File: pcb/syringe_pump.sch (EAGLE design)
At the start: 2 parts, among them U1 R-785.0-0.5

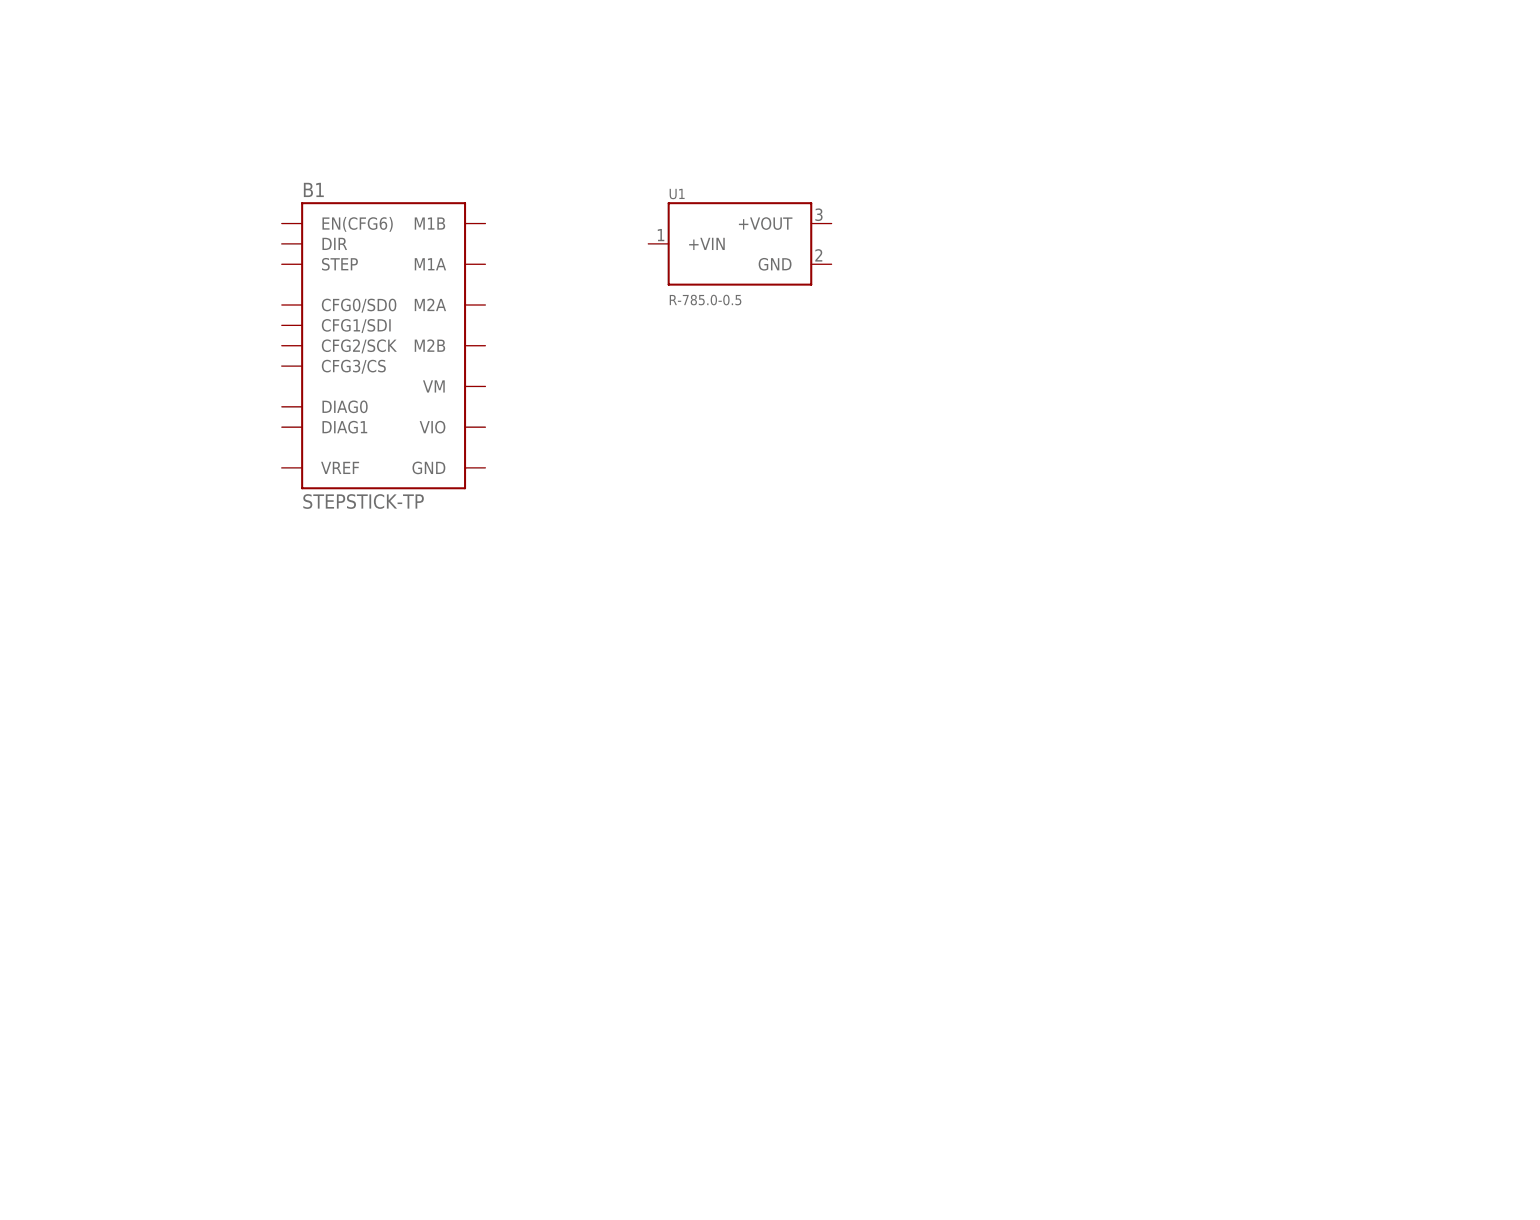
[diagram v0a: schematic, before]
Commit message: Completed syringe pump board and schematic.
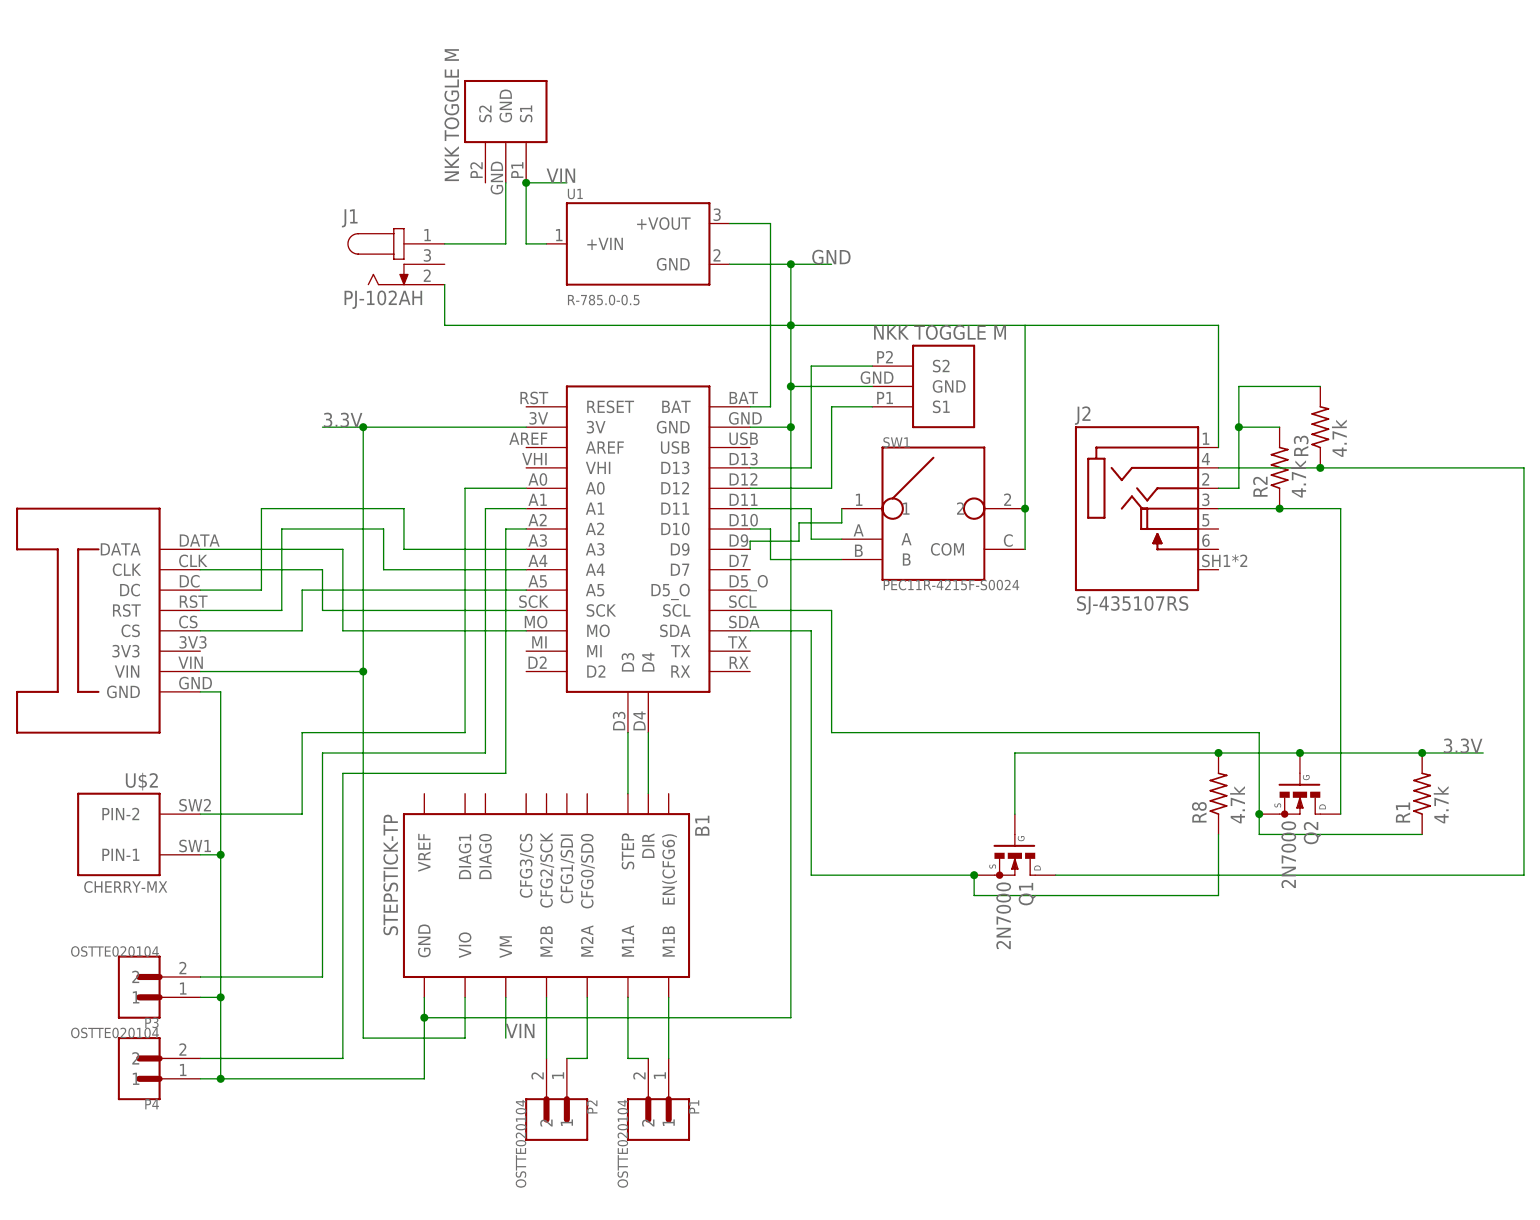
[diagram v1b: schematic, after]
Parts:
- added J1: PJ-102AH, PJ-102AH:PJ-102AH
- added J2: SJ-435107RS, SJ-435107RS:SJ-435107RS
- added P1, P2, P3, P4: OSTTE020104, OSTTE020104:OSTTE020104
- added Q1, Q2: 2N7000, 2N7000:2N7000
- added R1, R2, R3, R8: 4.7k, rcl:R-US_0207/10
- added SW1: PEC11R-4215F-S0024, PEC11R-4215F-S0024:PEC11R-4215F-S0024
- added U$1: ITSYBITSYM4, arthur:ITSYBITSYM4
- added U$2: CHERRY-MX, cherrymx:CHERRY-MX
- added U$3: OLED_128X64, arthur:OLED_128X64
- added U$4: NKK_M2012S2A2A30, arthur:NKK_M2012S2A2A30
- added U$5: NKK_B13AH, arthur:NKK_B13AH
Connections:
- new net 3.3V: B1.VIO, Q1.G, Q2.G, R1.2, R8.2, U$1.3V, U$3.VIN
- new net GND: B1.GND, J1.2, J2.SLEEVE, P3.1, P4.1, SW1.2, SW1.COM, U$1.GND, U$2.PIN-1, U$3.GND, U$5.GND, U1.GND
- new net N$1: Q1.S, R8.1, U$1.SDA
- new net N$10: J2.RING1, Q2.D, R2.1
- new net N$11: J2.RING2, Q1.D, R3.1
- new net N$12: U$1.MO, U$3.DATA
- new net N$13: U$1.A3, U$3.DC
- new net N$14: U$1.A5, U$3.CS
- new net N$15: U$1.A4, U$3.RST
- new net N$16: P4.2, U$1.A2
- new net N$17: U$1.SCK, U$3.CLK
- new net N$18: J1.1, U$4.GND
- new net N$19: P3.2, U$1.A1
- new net N$2: J2.TIP, R2.2, R3.2
- new net N$20: U$1.A0, U$2.PIN-2
- new net N$21: U$1.D12, U$5.S1
- new net N$22: U$1.D13, U$5.S2
- new net N$23: SW1.A, U$1.D11
- new net N$24: SW1.B, U$1.D10
- new net N$25: SW1.1, U$1.D9
- new net N$26: U$1.BAT, U1.+VOUT
- new net N$3: B1.STEP, U$1.D3
- new net N$4: B1.DIR, U$1.D4
- new net N$5: Q2.S, R1.1, U$1.SCL
- new net N$6: B1.M2B, P2.2
- new net N$7: B1.M2A, P2.1
- new net N$8: B1.M1B, P1.1
- new net N$9: B1.M1A, P1.2
- new net VIN: B1.VM, U$4.S1, U1.+VIN
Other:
- moved on the sheet: B1, U1

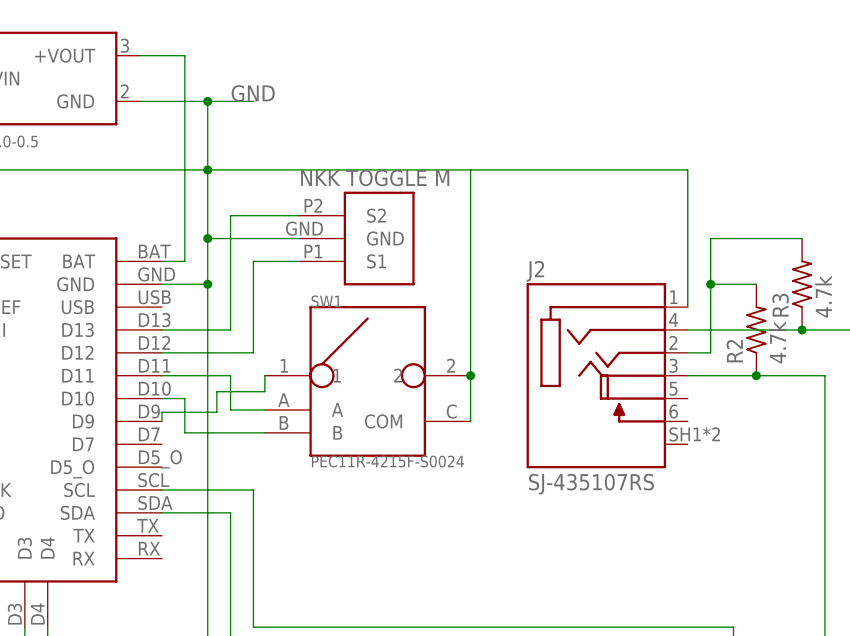
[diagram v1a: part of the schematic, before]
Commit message: Updated spacing of syringe pump and added copy of encoder library due to version issues.
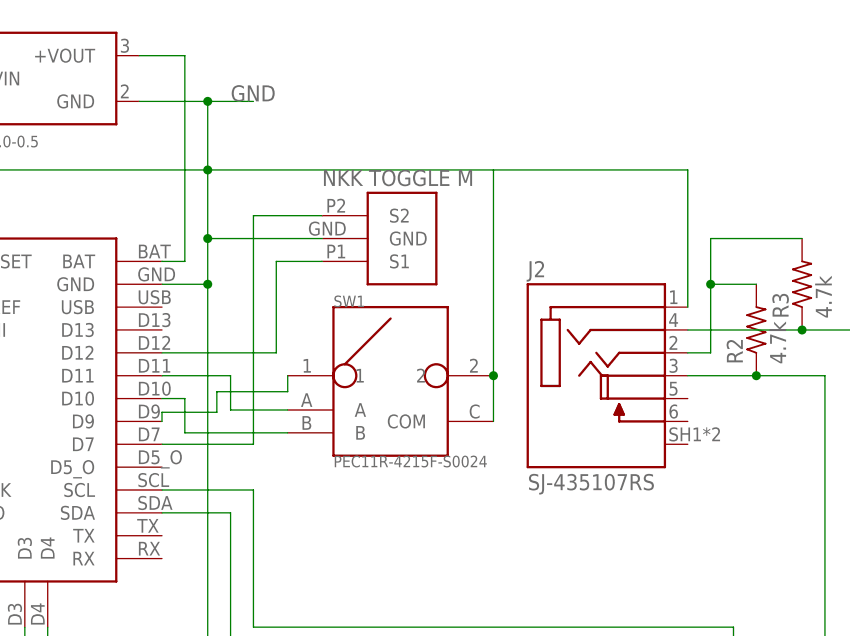
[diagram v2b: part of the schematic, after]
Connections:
- net N$22: now also U$1.D7; no longer U$1.D13
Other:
- moved on the sheet: SW1
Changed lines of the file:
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@@
 <attribute name="VALUE" x="153.162" y="57.15" size="1.778" layer="96" rot="R90"/>
 </instance>
-<instance part="SW1" gate="G$1" x="101.6" y="50.8" smashed="yes">
-<attribute name="NAME" x="95.24856875" y="58.421709375" size="1.270290625" layer="95"/>
-<attribute name="VALUE" x="95.24396875" y="40.6304" size="1.271209375" layer="96"/>
+<instance part="SW1" gate="G$1" x="104.14" y="50.8" smashed="yes">
+<attribute name="NAME" x="97.78856875" y="58.421709375" size="1.270290625" layer="95"/>
+<attribute name="VALUE" x="97.78396875" y="40.6304" size="1.271209375" layer="96"/>
 </instance>
 <instance part="U$4" gate="G$1" x="48.26" y="93.98" smashed="yes" rot="MR90"/>
-<instance part="U$5" gate="G$1" x="96.52" y="66.04" smashed="yes" rot="MR180"/>
+<instance part="U$5" gate="G$1" x="99.06" y="66.04" smashed="yes" rot="MR180"/>
 </instances>
 <busses>
@@
 <pinref part="J2" gate="G$1" pin="SLEEVE"/>
 <wire x1="137.16" y1="58.42" x2="137.16" y2="73.66" width="0.1524" layer="91"/>
-<wire x1="137.16" y1="73.66" x2="113.03" y2="73.66" width="0.1524" layer="91"/>
+<wire x1="137.16" y1="73.66" x2="115.57" y2="73.66" width="0.1524" layer="91"/>
 <pinref part="P3" gate="G$1" pin="1"/>
 <pinref part="P4" gate="G$1" pin="1"/>
-<wire x1="113.03" y1="73.66" x2="83.82" y2="73.66" width="0.1524" layer="91"/>
+<wire x1="115.57" y1="73.66" x2="83.82" y2="73.66" width="0.1524" layer="91"/>
 <wire x1="38.1" y1="-20.32" x2="38.1" y2="-12.7" width="0.1524" layer="91"/>
 <wire x1="12.7" y1="-20.32" x2="10.16" y2="-20.32" width="0.1524" layer="91"/>
@@
 <pinref part="SW1" gate="G$1" pin="COM"/>
 <pinref part="SW1" gate="G$1" pin="2"/>
-<wire x1="113.03" y1="45.72" x2="113.03" y2="50.8" width="0.1524" layer="91"/>
-<wire x1="113.03" y1="50.8" x2="113.03" y2="73.66" width="0.1524" layer="91"/>
-<junction x="113.03" y="50.8"/>
+<wire x1="115.57" y1="45.72" x2="115.57" y2="50.8" width="0.1524" layer="91"/>
+<wire x1="115.57" y1="50.8" x2="115.57" y2="73.66" width="0.1524" layer="91"/>
+<junction x="115.57" y="50.8"/>
 <pinref part="U$5" gate="G$1" pin="GND"/>
-<wire x1="93.98" y1="66.04" x2="83.82" y2="66.04" width="0.1524" layer="91"/>
+<wire x1="96.52" y1="66.04" x2="83.82" y2="66.04" width="0.1524" layer="91"/>
 <junction x="83.82" y="66.04"/>
 </segment>
@@
 </segment>
 </net>
-<net name="N$22" class="0">
-<segment>
-<pinref part="U$5" gate="G$1" pin="S2"/>
-<wire x1="93.98" y1="68.58" x2="86.36" y2="68.58" width="0.1524" layer="91"/>
-<wire x1="86.36" y1="68.58" x2="86.36" y2="55.88" width="0.1524" layer="91"/>
-<pinref part="U$1" gate="G$1" pin="D13"/>
-<wire x1="86.36" y1="55.88" x2="78.74" y2="55.88" width="0.1524" layer="91"/>
-</segment>
-</net>
 <net name="N$21" class="0">
 <segment>
 <pinref part="U$1" gate="G$1" pin="D12"/>
-<wire x1="78.74" y1="53.34" x2="88.9" y2="53.34" width="0.1524" layer="91"/>
-<wire x1="88.9" y1="53.34" x2="88.9" y2="63.5" width="0.1524" layer="91"/>
+<wire x1="78.74" y1="53.34" x2="91.44" y2="53.34" width="0.1524" layer="91"/>
+<wire x1="91.44" y1="53.34" x2="91.44" y2="63.5" width="0.1524" layer="91"/>
 <pinref part="U$5" gate="G$1" pin="S1"/>
-<wire x1="88.9" y1="63.5" x2="93.98" y2="63.5" width="0.1524" layer="91"/>
+<wire x1="91.44" y1="63.5" x2="96.52" y2="63.5" width="0.1524" layer="91"/>
 </segment>
 </net>
@@
 <pinref part="SW1" gate="G$1" pin="A"/>
 <wire x1="86.36" y1="50.8" x2="86.36" y2="46.99" width="0.1524" layer="91"/>
-<wire x1="86.36" y1="46.99" x2="90.17" y2="46.99" width="0.1524" layer="91"/>
+<wire x1="86.36" y1="46.99" x2="92.71" y2="46.99" width="0.1524" layer="91"/>
 </segment>
 </net>
@@
 <segment>
 <pinref part="SW1" gate="G$1" pin="B"/>
-<wire x1="90.17" y1="44.45" x2="81.28" y2="44.45" width="0.1524" layer="91"/>
+<wire x1="92.71" y1="44.45" x2="81.28" y2="44.45" width="0.1524" layer="91"/>
 <wire x1="81.28" y1="44.45" x2="81.28" y2="48.26" width="0.1524" layer="91"/>
 <pinref part="U$1" gate="G$1" pin="D10"/>
@@
 <wire x1="78.74" y1="46.736" x2="84.836" y2="46.736" width="0.1524" layer="91"/>
 <wire x1="84.836" y1="46.736" x2="84.836" y2="49.022" width="0.1524" layer="91"/>
-<wire x1="84.836" y1="49.022" x2="90.17" y2="49.022" width="0.1524" layer="91"/>
+<wire x1="84.836" y1="49.022" x2="92.71" y2="49.022" width="0.1524" layer="91"/>
 <pinref part="SW1" gate="G$1" pin="1"/>
-<wire x1="90.17" y1="49.022" x2="90.17" y2="50.8" width="0.1524" layer="91"/>
+<wire x1="92.71" y1="49.022" x2="92.71" y2="50.8" width="0.1524" layer="91"/>
 </segment>
 </net>
@@
 </segment>
 </net>
+<net name="N$22" class="0">
+<segment>
+<pinref part="U$1" gate="G$1" pin="D7"/>
+<wire x1="78.74" y1="43.18" x2="88.9" y2="43.18" width="0.1524" layer="91"/>
+<pinref part="U$5" gate="G$1" pin="S2"/>
+<wire x1="88.9" y1="43.18" x2="88.9" y2="68.58" width="0.1524" layer="91"/>
+<wire x1="88.9" y1="68.58" x2="96.52" y2="68.58" width="0.1524" layer="91"/>
+</segment>
+</net>
